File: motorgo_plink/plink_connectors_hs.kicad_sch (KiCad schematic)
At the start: 13 parts, among them J12 BM05B-SRSS-TB_LF__SN_, J13 BM05B-SRSS-TB_LF__SN_, J3 I2C_STANDARDQWIIC, J4 Conn_02x20_Odd_Even, J5 I2C_STANDARDQWIIC

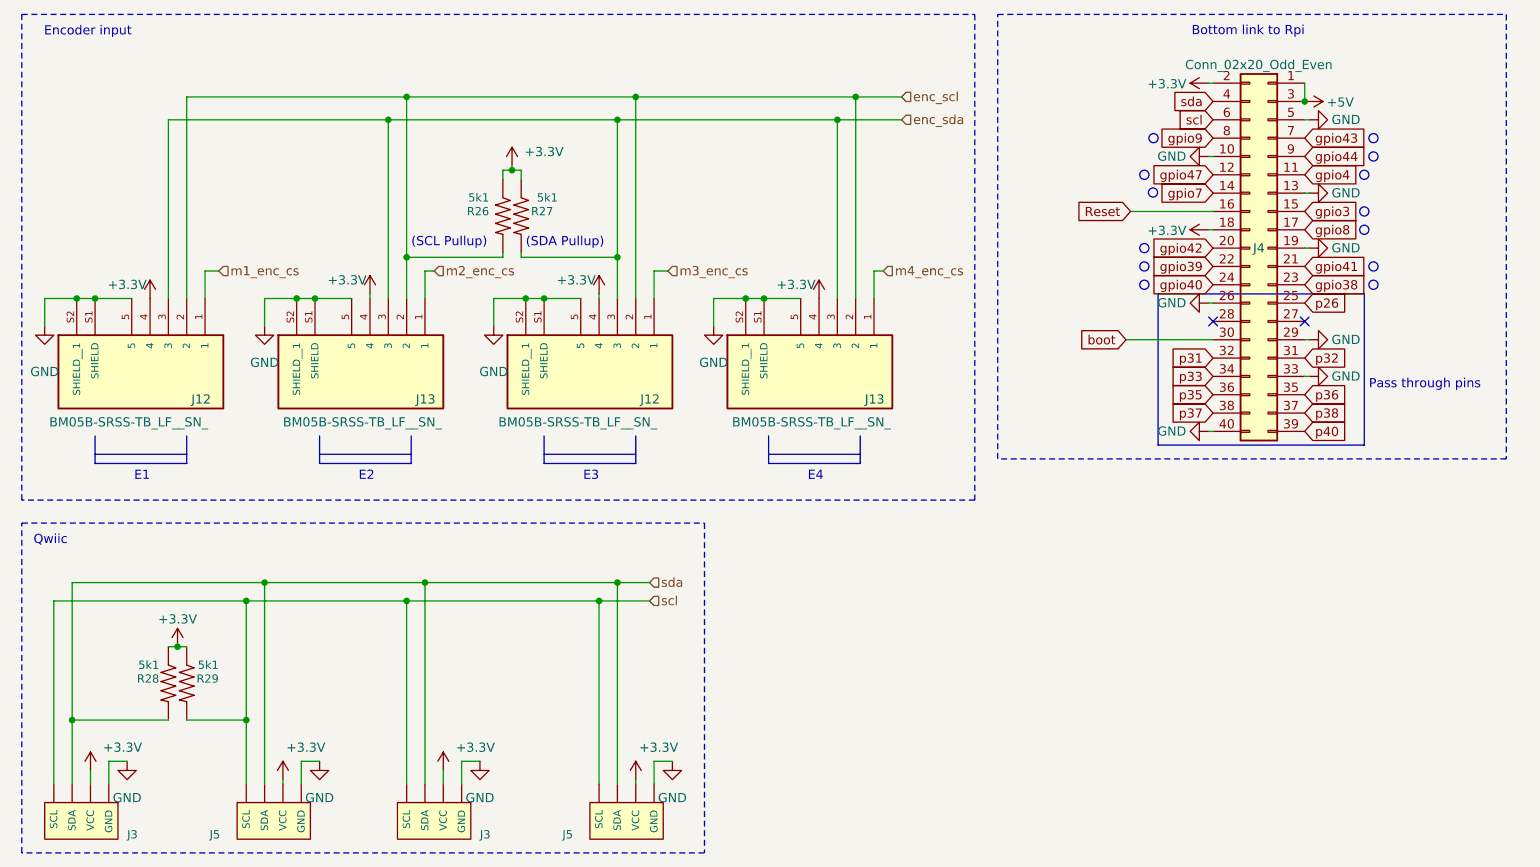
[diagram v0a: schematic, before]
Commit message: wip culling of non-vital schematic components
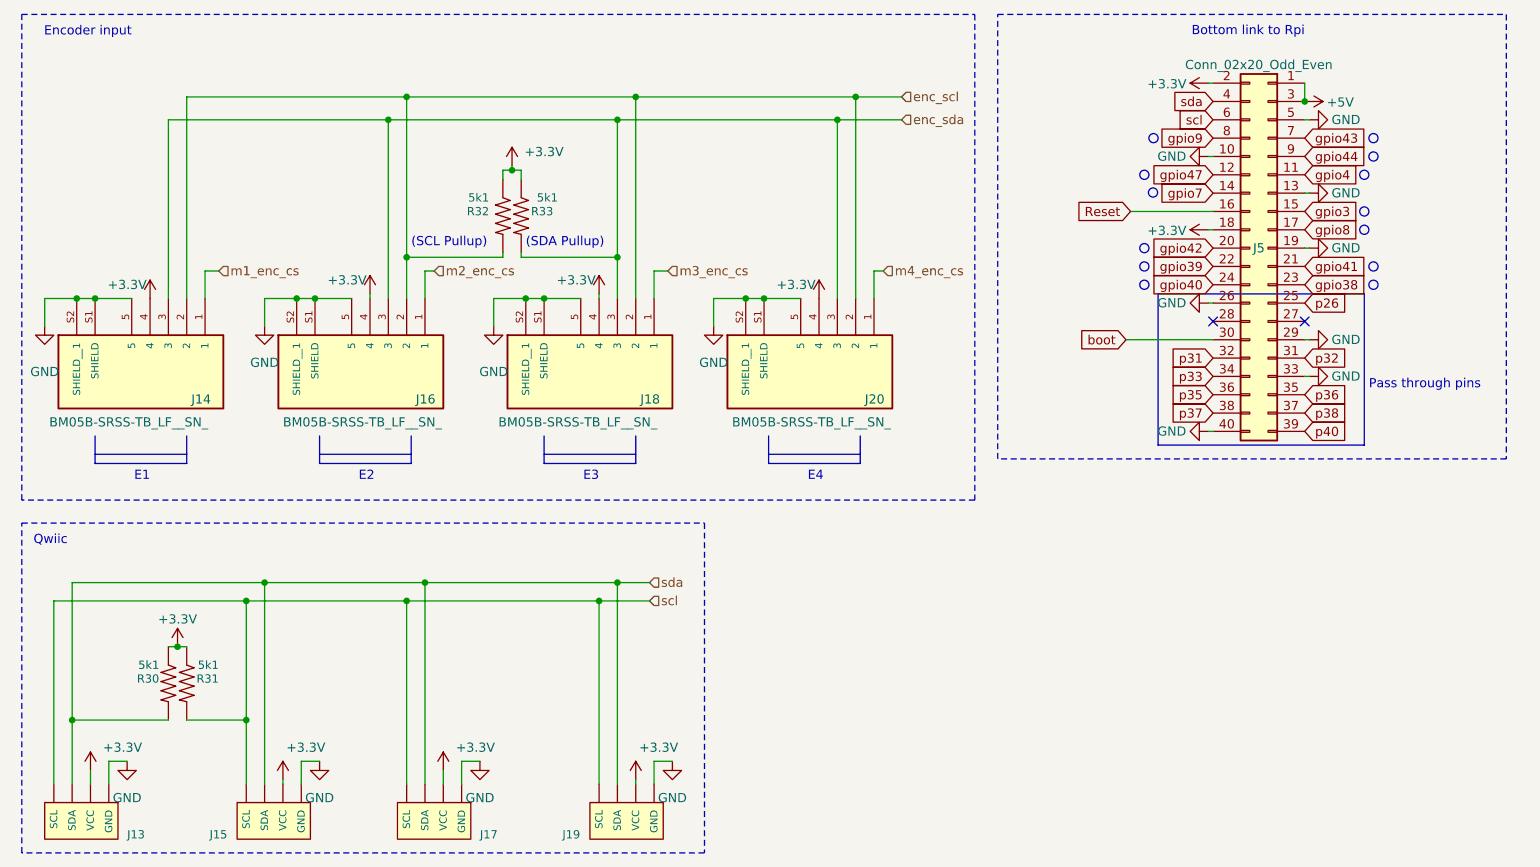
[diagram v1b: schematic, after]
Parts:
- renumbered J3 to J13, J12 to J14, J5 to J15, J13 to J16, J3 to J17, J12 to J18, J5 to J19, J13 to J20, J4 to J5, R28 to R30, R29 to R31, R26 to R32, R27 to R33

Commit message: wip culling schematics and removing tracks
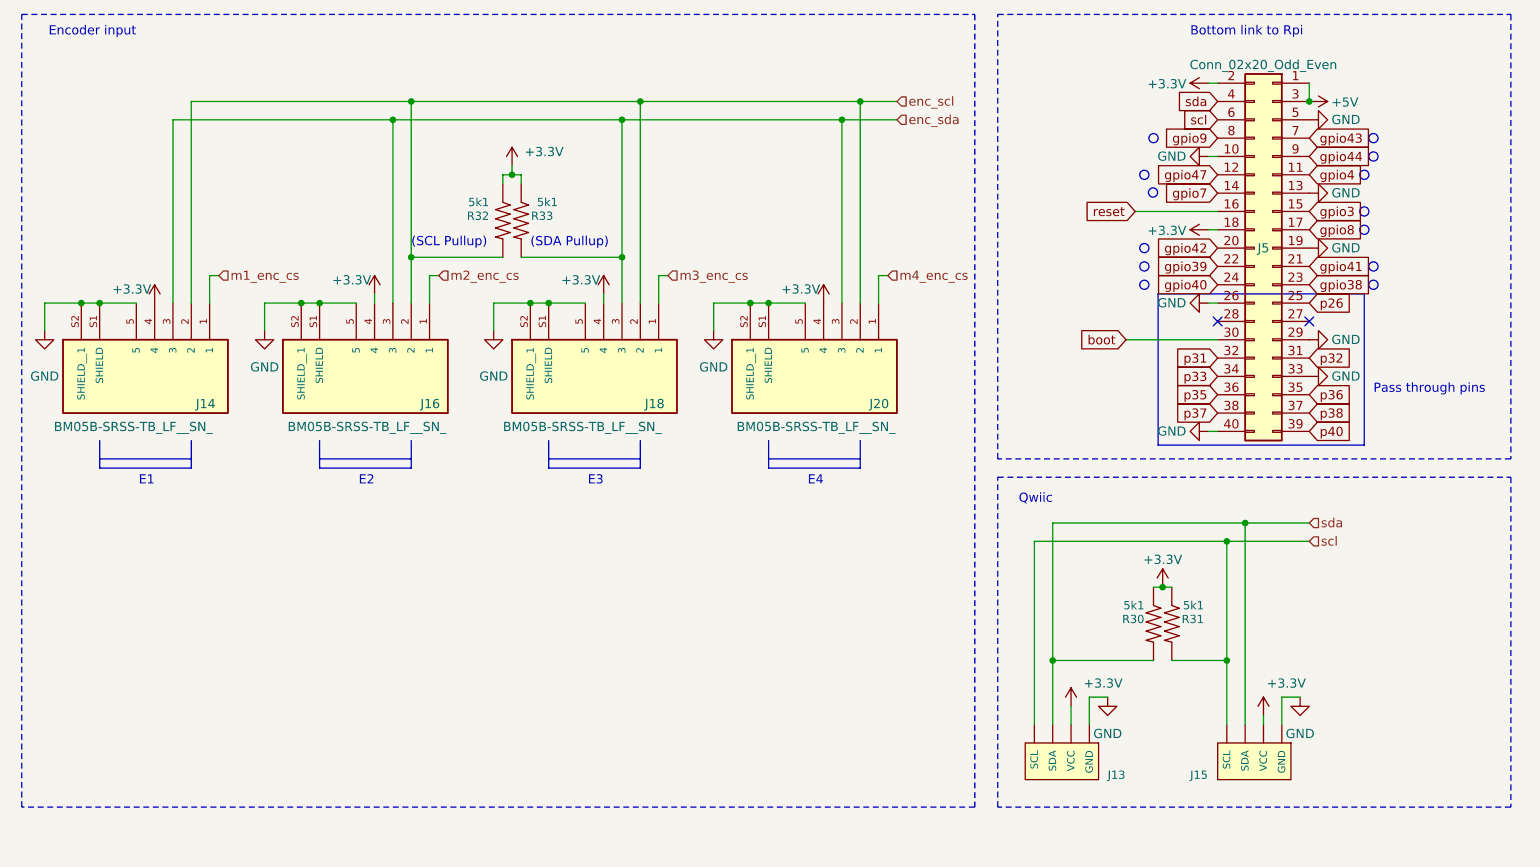
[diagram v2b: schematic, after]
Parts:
- removed J17, J19: I2C_STANDARDQWIIC, Connector_JST:JST_SH_BM04B-SRSS-TB_1x04-1MP_P1.00mm_Vertical, symbol sparkfun_connectors:I2C_STANDARDQWIIC
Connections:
- net Reset renamed reset
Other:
- moved on the sheet: J13, J14, J15, J16, J18, J20, J5, R30, R31, R32, R33

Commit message: layout complete! checkpoint ready for design review
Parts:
- removed J5: Conn_02x20_Odd_Even, Connector_PinSocket_2.54mm:PinSocket_2x20_P2.54mm_Vertical_SMD, symbol Connector_Generic:Conn_02x20_Odd_Even
- added J7: Conn_02x20_Odd_Even, Connector_PinSocket_2.54mm:PinSocket_2x20_P2.54mm_Vertical_SMD, symbol Connector_Generic:Conn_02x20_Odd_Even
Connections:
- net +5V: now also J7.2 (Pin_2), J7.4 (Pin_4)
- net GND: now also J7.14 (Pin_14), J7.20 (Pin_20), J7.25 (Pin_25), J7.30 (Pin_30), J7.34 (Pin_34), J7.39 (Pin_39), J7.6 (Pin_6), J7.9 (Pin_9)
- net boot: now also J7.29 (Pin_29)
- net gpio38: now also J7.18 (Pin_18)
- net gpio39: now also J7.11 (Pin_11)
- net gpio40: now also J7.16 (Pin_16)
- net gpio41: now also J7.12 (Pin_12)
- net gpio42: now also J7.10 (Pin_10)
- net gpio43: now also J7.8 (Pin_8)
- net gpio44: now also J7.7 (Pin_7)
- net gpio47: now also J7.23 (Pin_23)
- net p26: now also J7.26 (Pin_26)
- net p31: now also J7.31 (Pin_31)
- net p32: now also J7.32 (Pin_32)
- net p33: now also J7.33 (Pin_33)
- net p35: now also J7.35 (Pin_35)
- net p36: now also J7.36 (Pin_36)
- net p37: now also J7.37 (Pin_37)
- net p38: now also J7.38 (Pin_38)
- net p40: now also J7.40 (Pin_40)
- net reset: now also J7.15 (Pin_15)
- net scl: now also J7.5 (Pin_5)
- net sda: now also J7.3 (Pin_3)
- new net gpio21: J7.24 (Pin_24)
- new net gpio35: J7.19 (Pin_19)
- new net gpio36: J7.22 (Pin_22)
- new net gpio37: J7.13 (Pin_13)
- new net gpio48: J7.21 (Pin_21)
- no-connect marks 2 -> 4

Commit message: production files and all edits for final send off of v1.0
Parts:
- R30, R31, R32, R33: LCSC_Part_Number C409700 -> C25905
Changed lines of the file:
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@@
 			)
 		)
-		(property "LCSC_Part_Number" "C409700"
+		(property "LCSC_Part_Number" "C25905"
 			(at 95.25 49.53 0)
 			(effects
@@
 			)
 		)
-		(property "LCSC_Part_Number" "C409700"
+		(property "LCSC_Part_Number" "C25905"
 			(at 187.96 105.41 0)
 			(effects
@@
 			)
 		)
-		(property "LCSC_Part_Number" "C409700"
+		(property "LCSC_Part_Number" "C25905"
 			(at 185.42 105.41 0)
 			(effects
@@
 			)
 		)
-		(property "LCSC_Part_Number" "C409700"
+		(property "LCSC_Part_Number" "C25905"
 			(at 97.79 49.53 0)
 			(effects

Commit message: update to recent production files
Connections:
- net gpio42: now also J7.7 (Pin_7); no longer J7.10 (Pin_10)
- net gpio43: now also J7.10 (Pin_10); no longer J7.8 (Pin_8)
- net gpio44: now also J7.8 (Pin_8); no longer J7.7 (Pin_7)
